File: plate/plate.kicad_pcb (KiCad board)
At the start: 2 copper layers, 157.6 x 114.5 mm, 8 parts, among them J1 Conn_01x06, J2 Conn_01x06, J3 Conn_01x06, J4 Conn_01x06, J5 Conn_01x06, J6 Conn_01x06

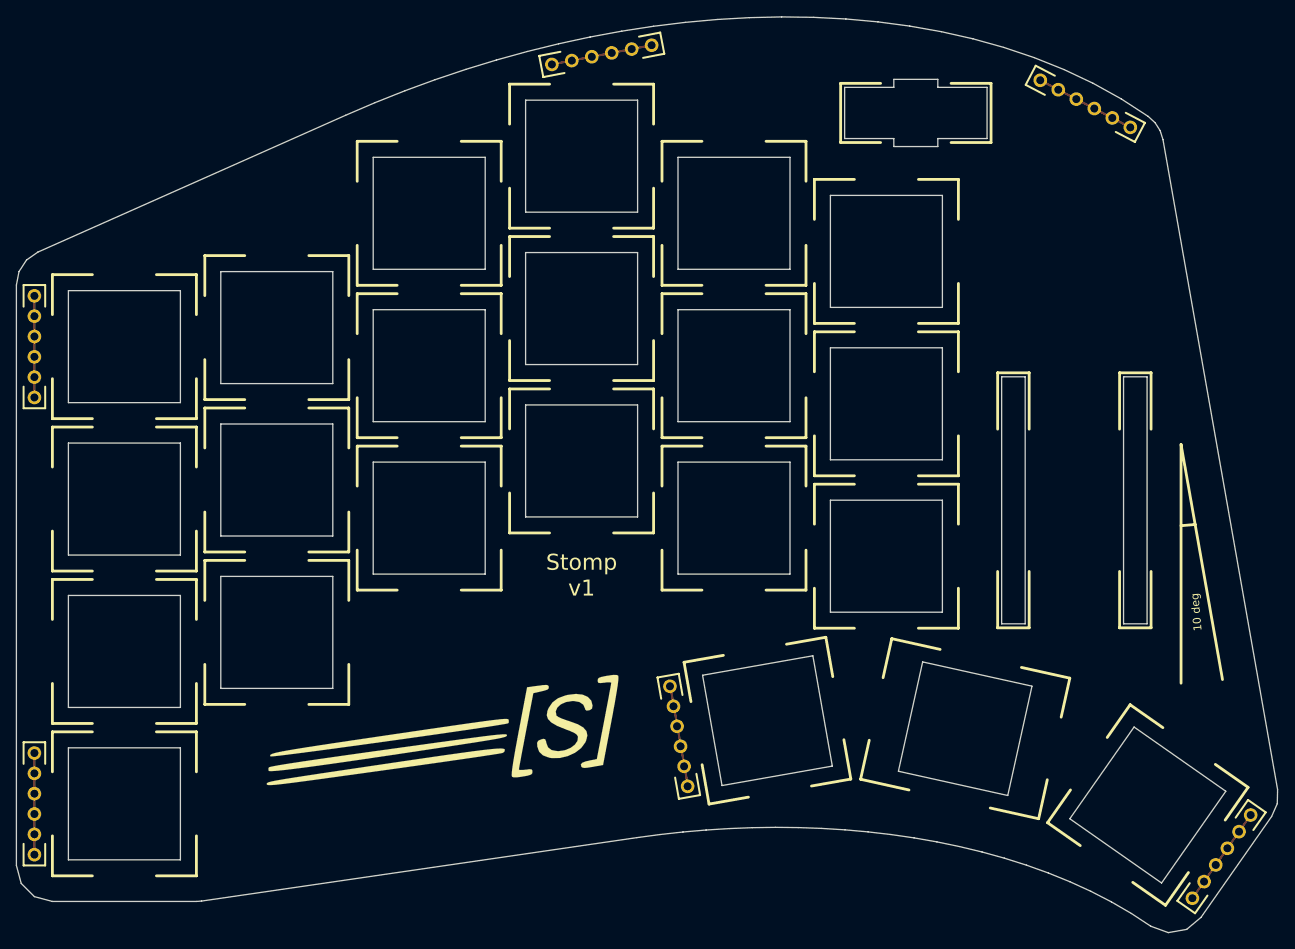
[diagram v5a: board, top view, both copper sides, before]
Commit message: Add higher resolution outline curves and magnet supports
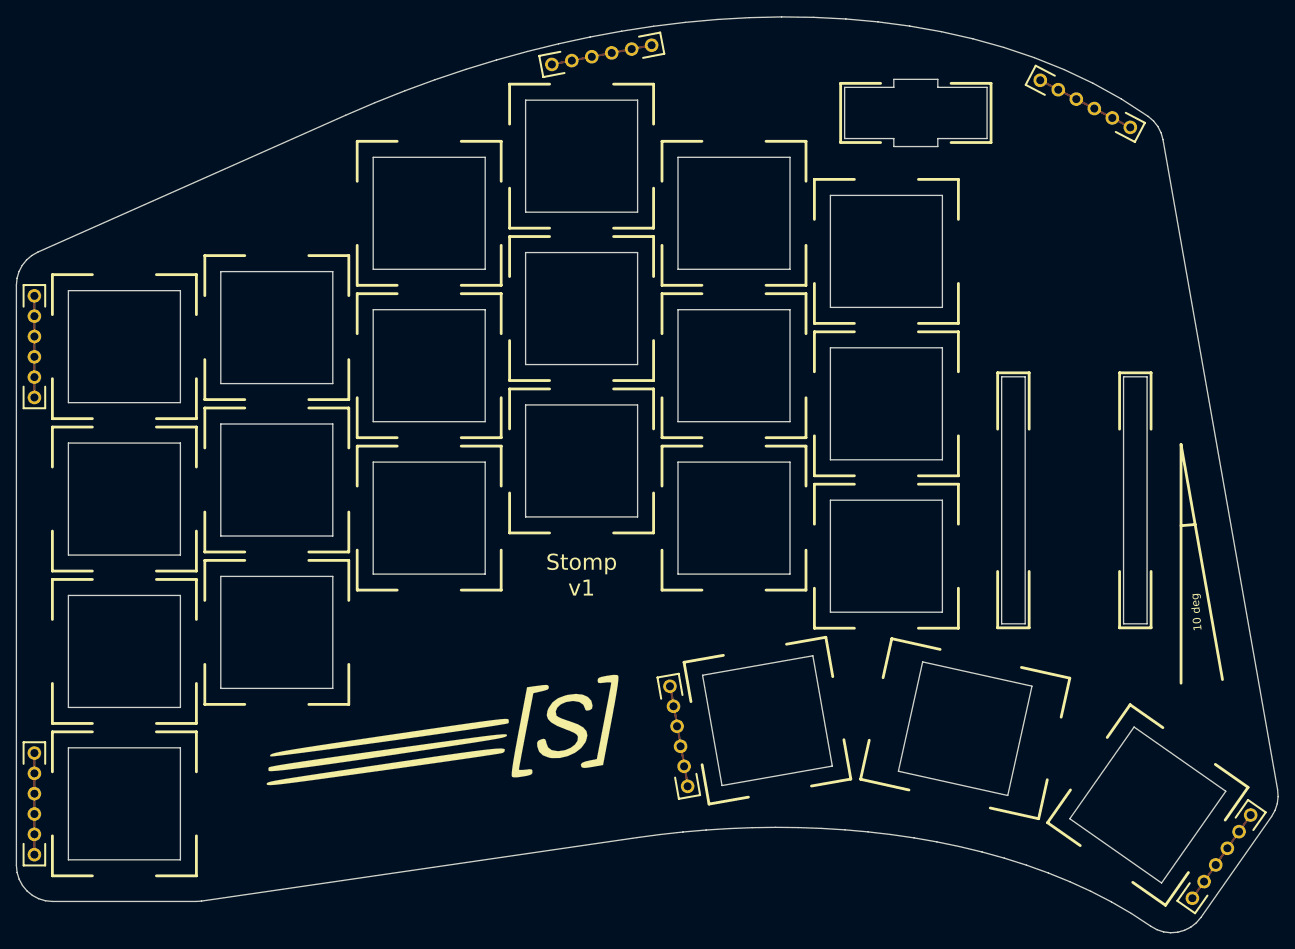
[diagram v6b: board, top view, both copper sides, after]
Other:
- board size 157.6 x 114.5 mm -> 157.7 x 114.5 mm

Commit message: Add mcu-dummy for secondary side and new logos on plate
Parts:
- removed the G*** at (-64.8, 13.8) (x2)
- added G***: LOGO, logos:plate-logo-right, B.Cu at (14.0, -26.2)
- added G***: LOGO, logos:plate-logo-left, F.Cu at (14.0, -26.2)
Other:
- board text removed: "10 deg"
